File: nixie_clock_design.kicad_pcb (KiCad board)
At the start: 2 copper layers, 160 x 60 mm, 124 parts, among them Q1 MPSA92, Q10 MPSA92, Q11 MPSA92, Q12 MPSA92, Q13 BSS138, Q14 UMH3N, Q15 IPD50R3K0CE, Q16 BSS138, Q17 BSS138, Q18 BSS138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

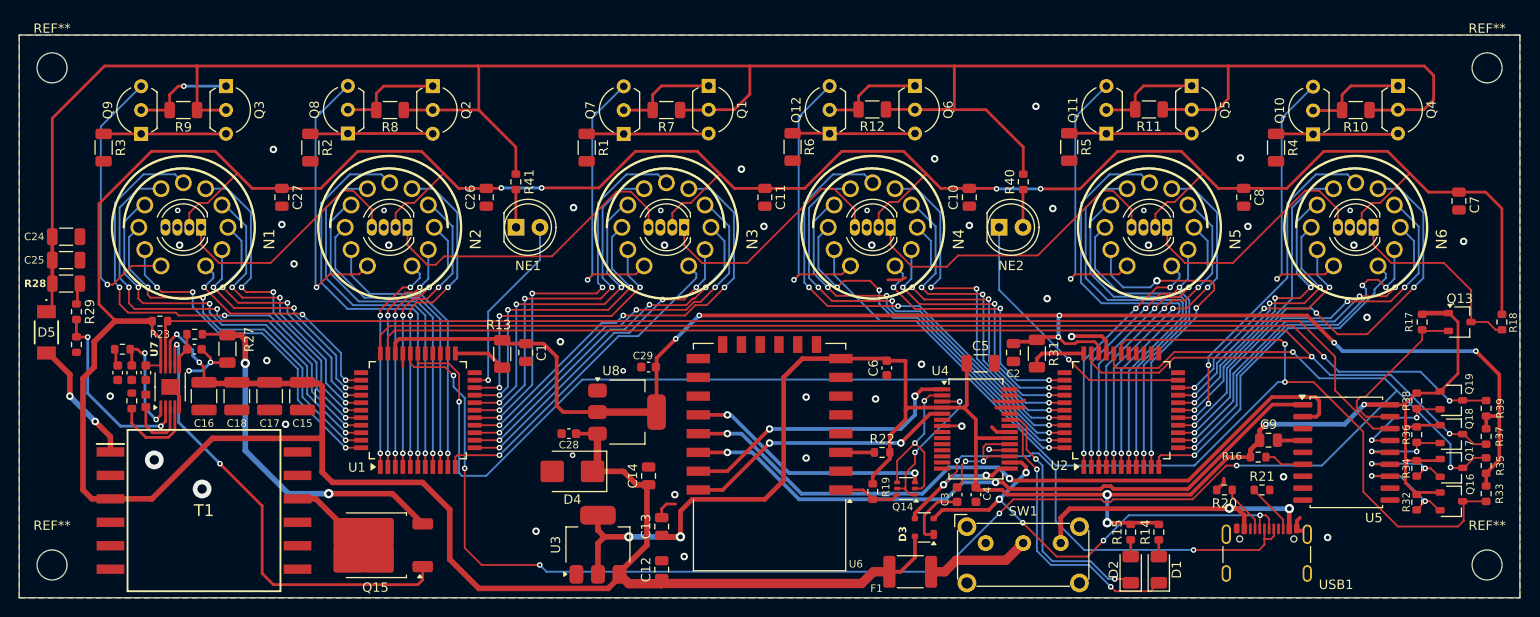
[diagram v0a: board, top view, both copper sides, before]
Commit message: fixed pull-ups
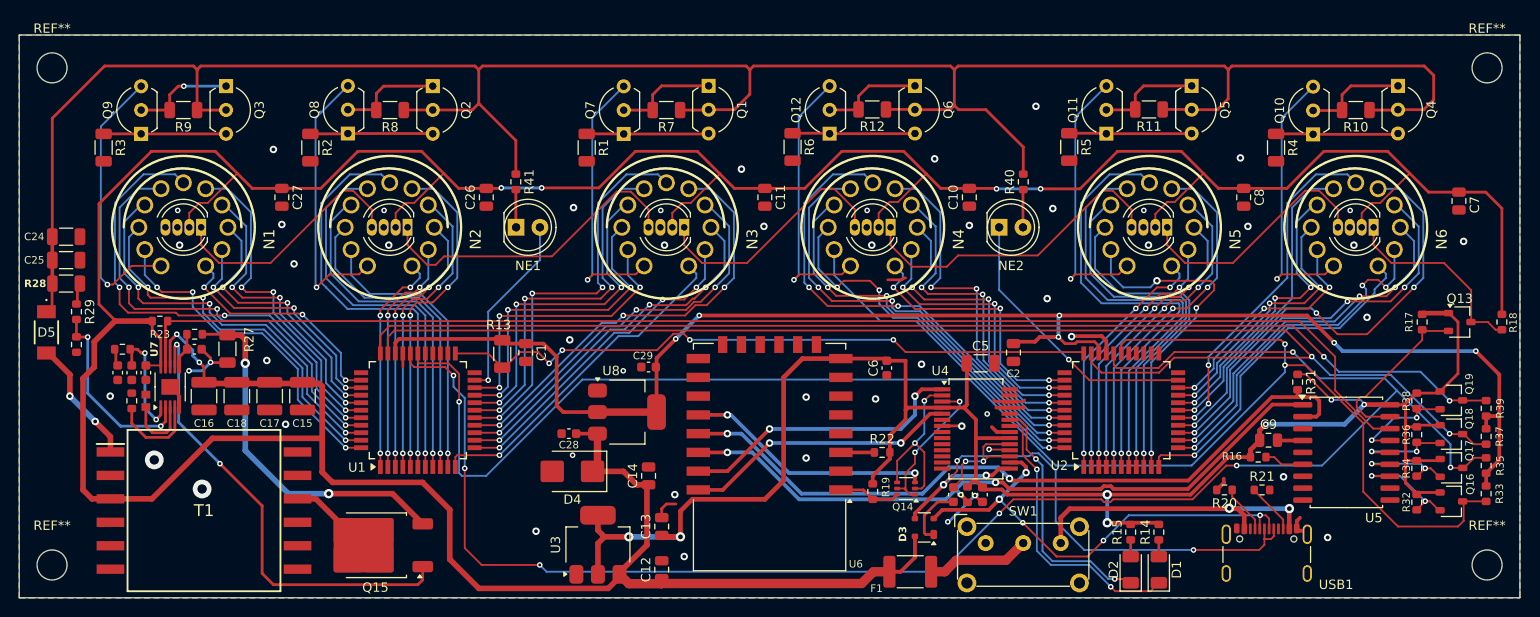
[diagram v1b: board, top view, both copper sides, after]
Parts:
- added R42: 4.7k, Resistor_SMD:R_0603_1608Metric, F.Cu at (181.2, 118.0)
- R31: value 10K -> 4.7k; footprint Resistor_SMD:R_1206_3216Metric -> Resistor_SMD:R_0603_1608Metric
- moved R31 28.0 mm to (216.4, 106.0)
- moved C4 0.70 mm to (182.8, 118.0)
- moved C3 0.40 mm to (179.7, 118.0)
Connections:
- R31 pad 1: +12V -> +3V3
- R31 pad 2: Net-(U2-DATAIN) -> Net-(U5-SDA)
- U2 pad 33: Net-(U2-DATAIN) -> Net-(U1-DATAOUT)
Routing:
- net Net-(U1-DATAOUT): track 5.63 -> 71.0 mm, vias 0 -> 4
- net +3V3: track 193.6 -> 202.8 mm, vias 6 -> 7
- net Net-(U2-DATAIN): track 6.15 -> 0.00 mm
- net GND: track 47.0 -> 51.8 mm, vias 49 -> 52
- net Net-(U5-SCL): track 71.5 -> 73.4 mm, vias 2 -> 3
- net +170V: track 257.2 -> 255.6 mm
- net Net-(U5-SDA): track 77.7 -> 78.5 mm
- net /Logic&PSU/HVOE: track 173.1 -> 173.8 mm

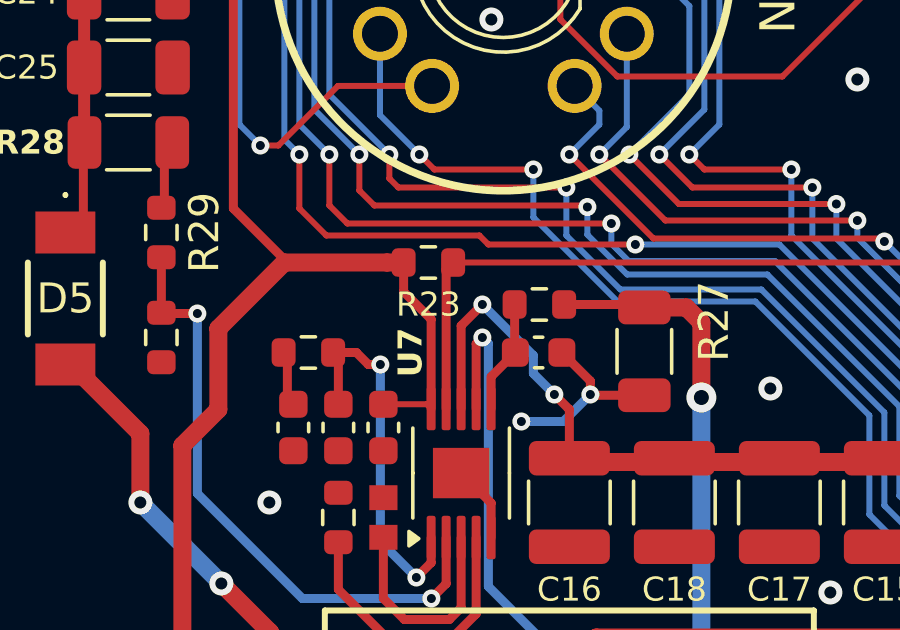
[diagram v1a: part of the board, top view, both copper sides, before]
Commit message: fixed 5V connection
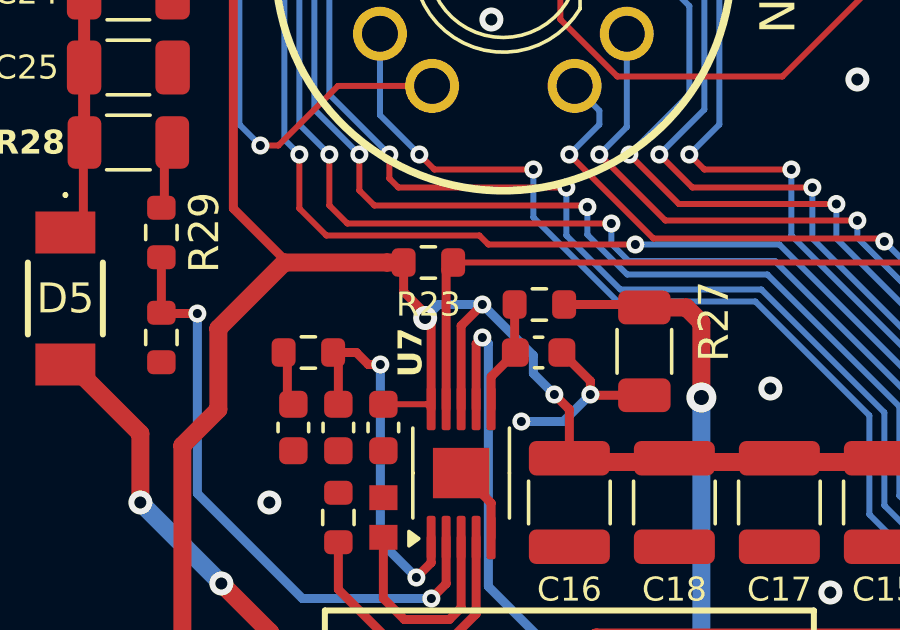
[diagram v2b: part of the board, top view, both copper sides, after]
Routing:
- net +5V: track 435.2 -> 437.3 mm, vias 6 -> 7
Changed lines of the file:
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@@
-	)
-	(segment
-		(start 96.9 100.9)
-		(end 96.1925 101.6075)
-		(width 0.3)
-		(layer "F.Cu")
-		(net 99)
 	)
 	(segment
@@
 	)
 	(segment
+		(start 96.9 100.9)
+		(end 96.1925 101.6075)
+		(width 0.3)
+		(layer "F.Cu")
+		(net 99)
+	)
+	(segment
 		(start 147.2 116.95)
 		(end 147.025 117.125)
@@
 	)
 	(segment
+		(start 96.1925 101.6075)
+		(end 96.1925 104.3675)
+		(width 0.3)
+		(layer "F.Cu")
+		(net 99)
+	)
+	(segment
 		(start 203.3 86.8)
 		(end 206.35 83.75)
@@
 		(start 228.35 83.75)
 		(end 230.35 85.75)
-		(width 0.3)
-		(layer "F.Cu")
-		(net 99)
-	)
-	(segment
-		(start 96.1925 101.6075)
-		(end 96.1925 104.3675)
 		(width 0.3)
 		(layer "F.Cu")
@@
 		(net 99)
 	)
+	(via
+		(at 94.9925 101.35)
+		(size 0.8)
+		(drill 0.4)
+		(layers "F.Cu" "B.Cu")
+		(net 99)
+	)
 	(segment
 		(start 99.3 103.9)
@@
 	)
 	(segment
+		(start 96.9 100.9)
+		(end 95.4425 100.9)
+		(width 0.3)
+		(layer "B.Cu")
+		(net 99)
+	)
+	(segment
 		(start 184.3 85.4)
 		(end 189 85.4)
@@
 		(width 0.3)
 		(layer "B.Cu")
+		(net 99)
+	)
+	(segment
+		(start 95.4425 100.9)
+		(end 94.9925 101.35)
+		(width 0.3)
+		(layer "B.Cu")

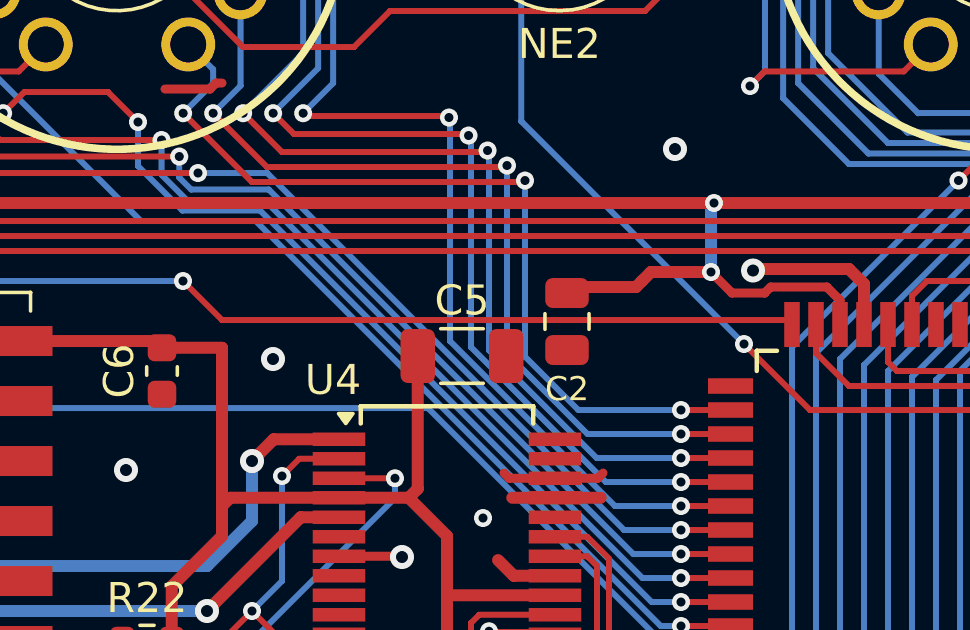
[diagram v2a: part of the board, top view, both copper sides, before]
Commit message: added HV5122 data line shunt
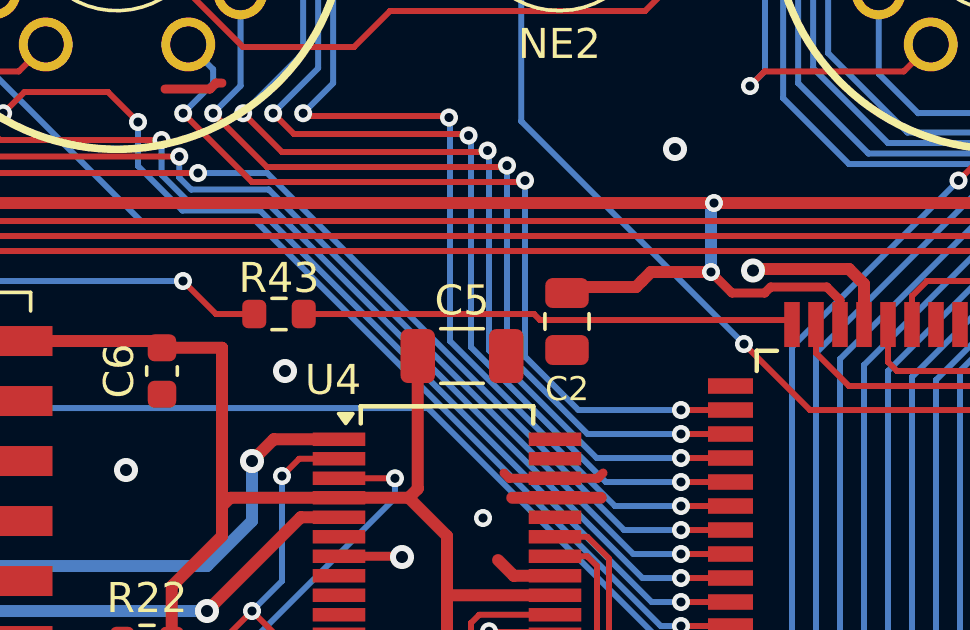
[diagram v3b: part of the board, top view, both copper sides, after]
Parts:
- added R43: 0, Resistor_SMD:R_0603_1608Metric, F.Cu at (176.5, 102.6)
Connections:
- U2 pad 33: Net-(U1-DATAOUT) -> Net-(U2-DATAIN)
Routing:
- net Net-(U1-DATAOUT): track 71.0 -> 52.9 mm
- net Net-(U2-DATAIN): track 0.00 -> 16.4 mm
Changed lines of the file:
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@@
 	(net 174 "Net-(LED4-DI)")
 	(net 175 "Net-(LED5-DI)")
+	(net 176 "Net-(U2-DATAIN)")
 	(footprint "Resistor_SMD:R_0603_1608Metric"
 		(layer "F.Cu")
@@
 	(footprint "Resistor_SMD:R_0603_1608Metric"
 		(layer "F.Cu")
+		(at 176.5 102.6)
+		(descr "Resistor SMD 0603 (1608 Metric), square (rectangular) end terminal, IPC_7351 nominal, (Body size source: IPC-SM-782 page 72, https://www.pcb-3d.com/wordpress/wp-content/uploads/ipc-sm-782a_amendment_1_and_2.pdf), generated with kicad-footprint-generator")
+		(tags "resistor")
+		(property "Reference" "R43"
+			(at 0 -1.2 0)
+			(layer "F.SilkS")
+			(effects
+				(font
+					(size 1 1)
+					(thickness 0.15)
+				)
+			)
+		)
+		(property "Value" "0"
+			(at 0 1.43 360)
+			(layer "F.Fab")
+			(hide yes)
+			(effects
+				(font
+					(size 1 1)
+					(thickness 0.15)
+				)
+			)
+		)
+		(property "Footprint" "Resistor_SMD:R_0603_1608Metric"
+			(at 0 0 0)
+			(unlocked yes)
+			(layer "F.Fab")
+			(hide yes)
+			(effects
+				(font
+					(size 1.27 1.27)
+				)
+			)
+		)
+		(property "Datasheet" ""
+			(at 0 0 0)
+			(unlocked yes)
+			(layer "F.Fab")
+			(hide yes)
+			(effects
+				(font
+					(size 1.27 1.27)
+				)
+			)
+		)
+		(property "Description" "Resistor"
+			(at 0 0 0)
+			(unlocked yes)
+			(layer "F.Fab")
+			(hide yes)
+			(effects
+				(font
+					(size 1.27 1.27)
+				)
+			)
+		)
+		(property "MPN" "MCT06030Z0000ZPW00"
+			(at 0 0 0)
+			(unlocked yes)
+			(layer "F.Fab")
+			(hide yes)
+			(effects
+				(font
+					(size 1 1)
+					(thickness 0.15)
+				)
+			)
+		)
+		(property ki_fp_filters "R_*")
+		(sheetname "Nixie Driver")
+		(sheetfile "nixie_driver.kicad_sch")
+		(attr smd)
+		(fp_line
+			(start -0.237258 -0.5225)
+			(end 0.237258 -0.5225)
+			(stroke
+				(width 0.12)
+				(type solid)
+			)
+			(layer "F.SilkS")
+		)
+		(fp_line
+			(start -0.237258 0.5225)
+			(end 0.237258 0.5225)
+			(stroke
+				(width 0.12)
+				(type solid)
+			)
+			(layer "F.SilkS")
+		)
+		(fp_line
+			(start -1.48 -0.73)
+			(end 1.48 -0.73)
+			(stroke
+				(width 0.05)
+				(type solid)
+			)
+			(layer "F.CrtYd")
+		)
+		(fp_line
+			(start -1.48 0.73)
+			(end -1.48 -0.73)
+			(stroke
+				(width 0.05)
+				(type solid)
+			)
+			(layer "F.CrtYd")
+		)
+		(fp_line
+			(start 1.48 -0.73)
+			(end 1.48 0.73)
+			(stroke
+				(width 0.05)
+				(type solid)
+			)
+			(layer "F.CrtYd")
+		)
+		(fp_line
+			(start 1.48 0.73)
+			(end -1.48 0.73)
+			(stroke
+				(width 0.05)
+				(type solid)
+			)
+			(layer "F.CrtYd")
+		)
+		(fp_line
+			(start -0.8 -0.4125)
+			(end 0.8 -0.4125)
+			(stroke
+				(width 0.1)
+				(type solid)
+			)
+			(layer "F.Fab")
+		)
+		(fp_line
+			(start -0.8 0.4125)
+			(end -0.8 -0.4125)
+			(stroke
+				(width 0.1)
+				(type solid)
+			)
+			(layer "F.Fab")
+		)
+		(fp_line
+			(start 0.8 -0.4125)
+			(end 0.8 0.4125)
+			(stroke
+				(width 0.1)
+				(type solid)
+			)
+			(layer "F.Fab")
+		)
+		(fp_line
+			(start 0.8 0.4125)
+			(end -0.8 0.4125)
+			(stroke
+				(width 0.1)
+				(type solid)
+			)
+			(layer "F.Fab")
+		)
+		(fp_text user "${REFERENCE}"
+			(at 0 0 360)
+			(layer "F.Fab")
+			(effects
+				(font
+					(size 0.4 0.4)
+					(thickness 0.06)
+				)
+			)
+		)
+		(pad "1" smd roundrect
+			(at -0.825 0)
+			(size 0.8 0.95)
+			(layers "F.Cu" "F.Paste" "F.Mask")
+			(roundrect_rratio 0.25)
+			(net 67 "Net-(U1-DATAOUT)")
+			(pintype "passive")
+		)
+		(pad "2" smd roundrect
+			(at 0.825 0)
+			(size 0.8 0.95)
+			(layers "F.Cu" "F.Paste" "F.Mask")
+			(roundrect_rratio 0.25)
+			(net 176 "Net-(U2-DATAIN)")
+			(pintype "passive")
+		)
+		(model "${KICAD8_3DMODEL_DIR}/Resistor_SMD.3dshapes/R_0603_1608Metric.wrl"
+			(offset
+				(xyz 0 0 0)
+			)
+			(scale
+				(xyz 1 1 1)
+			)
+			(rotate
+				(xyz 0 0 0)
+			)
+		)
+	)
+	(footprint "Resistor_SMD:R_0603_1608Metric"
+		(layer "F.Cu")
 		(at 229.1 111.6 -90)
 		(descr "Resistor SMD 0603 (1608 Metric), square (rectangular) end terminal, IPC_7351 nominal, (Body size source: IPC-SM-782 page 72, https://www.pcb-3d.com/wordpress/wp-content/uploads/ipc-sm-782a_amendment_1_and_2.pdf), generated with kicad-footprint-generator")
@@
 			(size 1.5 0.52)
 			(layers "F.Cu" "F.Paste" "F.Mask")
-			(net 67 "Net-(U1-DATAOUT)")
+			(net 176 "Net-(U2-DATAIN)")
 			(pinfunction "DATAIN")
 			(pintype "input")
@@
 	)
 	(via
-		(at 176.3 104.1)
+		(at 176.7 104.5)
 		(size 0.8)
 		(drill 0.4)
@@
 	)
 	(segment
-		(start 131.8375 104.4625)
-		(end 131.6 104.4625)
+		(start 173.3 101.5)
+		(end 174.4 102.6)
 		(width 0.2)
 		(layer "F.Cu")
@@
 	)
 	(segment
-		(start 126.6 102.95)
-		(end 130.0875 102.95)
+		(start 174.4 102.6)
+		(end 175.675 102.6)
 		(width 0.2)
 		(layer "F.Cu")
@@
 	)
 	(segment
-		(start 150.95 100.85)
-		(end 151.6 101.5)
+		(start 131.8375 104.4625)
+		(end 131.6 104.4625)
 		(width 0.2)
 		(layer "F.Cu")
@@
 	)
 	(segment
-		(start 173.3 101.5)
-		(end 174.6 102.8)
+		(start 126.6 102.95)
+		(end 130.0875 102.95)
 		(width 0.2)
 		(layer "F.Cu")
@@
 	)
 	(segment
-		(start 174.6 102.8)
-		(end 193.45 102.8)
+		(start 150.95 100.85)
+		(end 151.6 101.5)
 		(width 0.2)
 		(layer "F.Cu")
@@
 	)
 	(segment
-		(start 193.45 102.8)
-		(end 193.6 102.95)
-		(width 0.2)
-		(layer "F.Cu")
-		(net 67)
-	)
-	(segment
 		(start 138 102.6)
 		(end 148.1 102.6)
@@
 		(net 175)
 	)
+	(segment
+		(start 185.2 102.8)
+		(end 193.45 102.8)
+		(width 0.2)
+		(layer "F.Cu")
+		(net 176)
+	)
+	(segment
+		(start 193.45 102.8)
+		(end 193.6 102.95)
+		(width 0.2)
+		(layer "F.Cu")
+		(net 176)
+	)
+	(segment
+		(start 185 102.6)
+		(end 185.2 102.8)
+		(width 0.2)
+		(layer "F.Cu")
+		(net 176)
+	)
+	(segment
+		(start 177.325 102.6)
+		(end 185 102.6)
+		(width 0.2)
+		(layer "F.Cu")
+		(net 176)
+	)
 	(zone
